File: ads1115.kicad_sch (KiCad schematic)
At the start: 20 parts, among them J29 Conn_02x04_Odd_Even, J30 Conn_01x02, J31 Conn_01x02, J32 Conn_01x02, J33 Conn_01x02, J34 Conn_01x04, U20 ADS1115IDGS

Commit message: WIP v0.2.0 changes
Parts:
- removed J29: Conn_02x04_Odd_Even, HL_Connector_Pad_2.54mm:Pad_2x04_P2.54_1.7x1.7_Rect-Oct, symbol Connector_Generic:Conn_02x04_Odd_Even
- removed J34: Conn_01x04, HL_Connector_Pad_2.54mm:Pad_1x04_P2.54_1.7x1.7_Rect-Oct, symbol Connector_Generic:Conn_01x04
- removed R71, R72, R73, R74: 10k, Resistor_SMD:R_0603_1608Metric_Pad0.98x0.95mm_HandSolder, symbol Device:R
- added J100: Conn_01x05, HL_Connector_Pad_2.54mm:Pad_1x05_P2.54_1.7x1.7_Rect-Oct, symbol Connector_Generic:Conn_01x05
- J27: renamed from J30; footprint HL_Connector_Pad_2.00mm:Pad_1x02_P2.00_1.35x1.35_Oct -> HL_Connector_Pad_2.00mm:Pad_1x02_P2.00_1.35x1.35_Rect-Oct
- J28: renamed from J31; footprint HL_Connector_Pad_2.00mm:Pad_1x02_P2.00_1.35x1.35_Oct -> HL_Connector_Pad_2.00mm:Pad_1x02_P2.00_1.35x1.35_Rect-Oct
- J29: renamed from J32; footprint HL_Connector_Pad_2.00mm:Pad_1x02_P2.00_1.35x1.35_Oct -> HL_Connector_Pad_2.00mm:Pad_1x02_P2.00_1.35x1.35_Rect-Oct
- J30: renamed from J33; footprint HL_Connector_Pad_2.00mm:Pad_1x02_P2.00_1.35x1.35_Oct -> HL_Connector_Pad_2.00mm:Pad_1x02_P2.00_1.35x1.35_Rect-Oct
- R75, R76, R77, R78: value 1k -> 10k; LCSC C17513 -> C17414
- RV10, RV7, RV8, RV9: LCSC (none) -> C118963; THT_LCSC C118963 -> (none)
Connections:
- net AINc0: now also RV7.1, J100.2 (Pin_2); no longer J27.1 (Pin_1), RV7.2
- net AINc1: now also RV8.1, J100.3 (Pin_3); no longer J28.1 (Pin_1), RV8.2
- net AINc2: now also RV9.1, J100.4 (Pin_4); no longer J29.1 (Pin_1), RV9.2
- net AINc3: now also RV10.1, J100.5 (Pin_5); no longer J30.1 (Pin_1), RV10.2
- net AINr0: now also RV7.2; no longer RV7.3
- net AINr1: now also RV8.2; no longer RV8.3
- net AINr2: now also RV9.2; no longer RV9.3
- net AINr3: now also RV10.2; no longer RV10.3
- net GND: now also J27.1 (Pin_1), J28.1 (Pin_1), J29.1 (Pin_1), J30.1 (Pin_1), RV10.3, RV7.3, RV8.3, RV9.3, J100.1 (Pin_1)
- net ALERT/RDY renamed ALERT/RDY
- no-connect marks 4 -> 0
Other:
- moved on the sheet: J27, J28, J29, J30, RV10, RV7, RV8, RV9

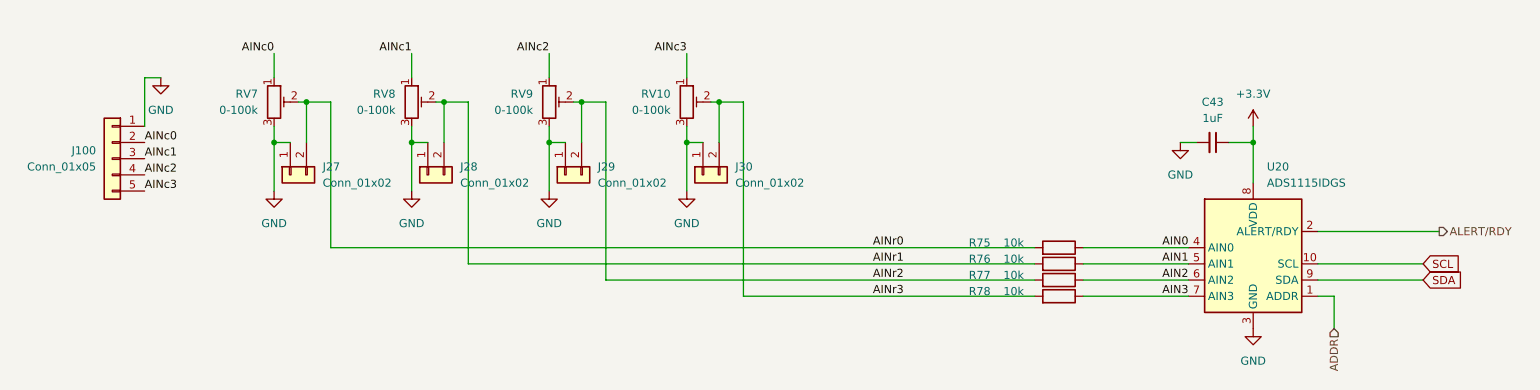
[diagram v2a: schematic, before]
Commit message: Assign part numbers and finish other 0.2.0 changes
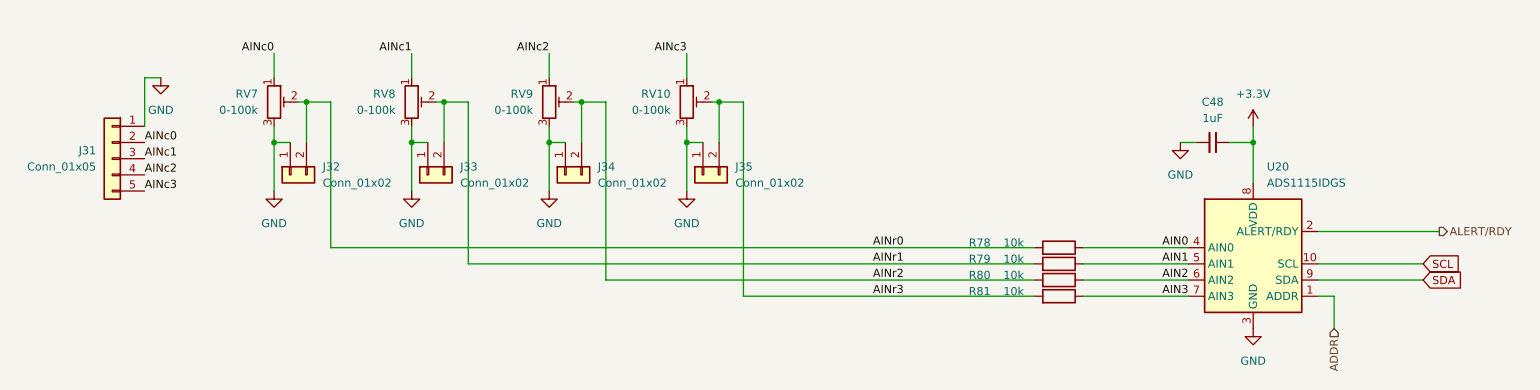
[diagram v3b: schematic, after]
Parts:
- J31: renamed from J100; LCSC (none) -> C492404
- renumbered C43 to C48, J27 to J32, J28 to J33, J29 to J34, J30 to J35, R75 to R78, R76 to R79, R77 to R80, R78 to R81

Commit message: Update the title blocks
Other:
- company: (none) -> Hat Labs Oy
- title: (none) -> HALSPA - Hat Labs Spaghetti Board
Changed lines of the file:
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@@
 	(generator_version "9.0")
 	(paper "A4")
+	(title_block
+		(title "HALSPA - Hat Labs Spaghetti Board")
+		(date "2025-04-17")
+		(rev "v0.2.0")
+		(company "Hat Labs Oy")
+		(comment 1 "See the accompanying LICENSE.md file for license details.")
+	)
 	(junction
 		(at 69.85 74.93)

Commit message: Fix minor production issues
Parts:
- J31: JLCPCB_CORRECTION (none) -> 0;5.08;270
- RV10, RV7, RV8, RV9: now in the parts list
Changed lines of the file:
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@@
 		(unit 1)
 		(exclude_from_sim no)
-		(in_bom no)
+		(in_bom yes)
 		(on_board yes)
 		(dnp no)
@@
 		(unit 1)
 		(exclude_from_sim no)
-		(in_bom no)
+		(in_bom yes)
 		(on_board yes)
 		(dnp no)
@@
 		(unit 1)
 		(exclude_from_sim no)
-		(in_bom no)
+		(in_bom yes)
 		(on_board yes)
 		(dnp no)
@@
 		(unit 1)
 		(exclude_from_sim no)
-		(in_bom no)
+		(in_bom yes)
 		(on_board yes)
 		(dnp no)
@@
 			(at 44.45 77.47 0)
 			(effects
+				(font
+					(size 1.27 1.27)
+				)
+				(hide yes)
+			)
+		)
+		(property "JLCPCB_CORRECTION" "0;5.08;270"
+			(at 44.45 77.47 0)
+			(effects

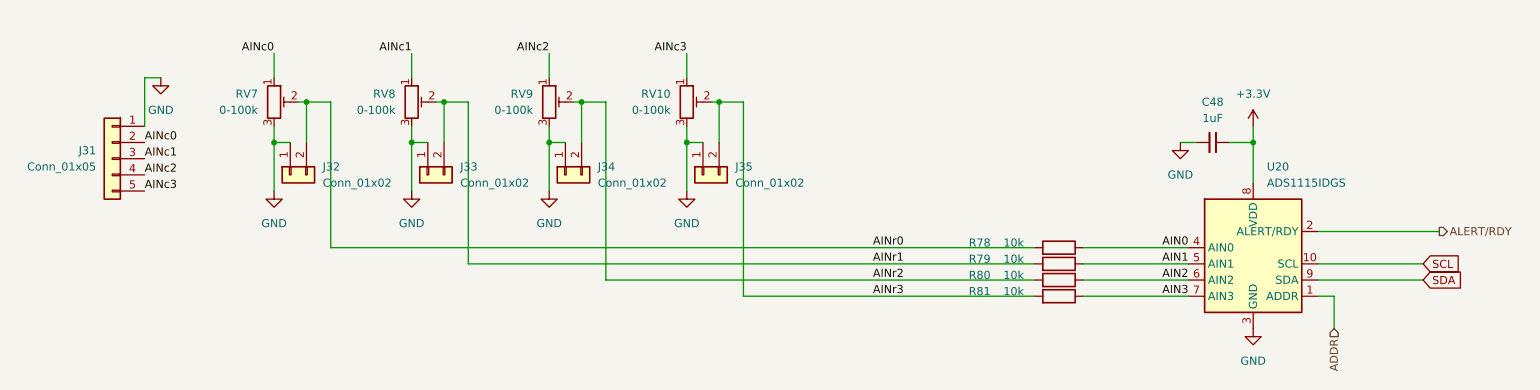
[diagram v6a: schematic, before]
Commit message: Adjust trimmer test pads
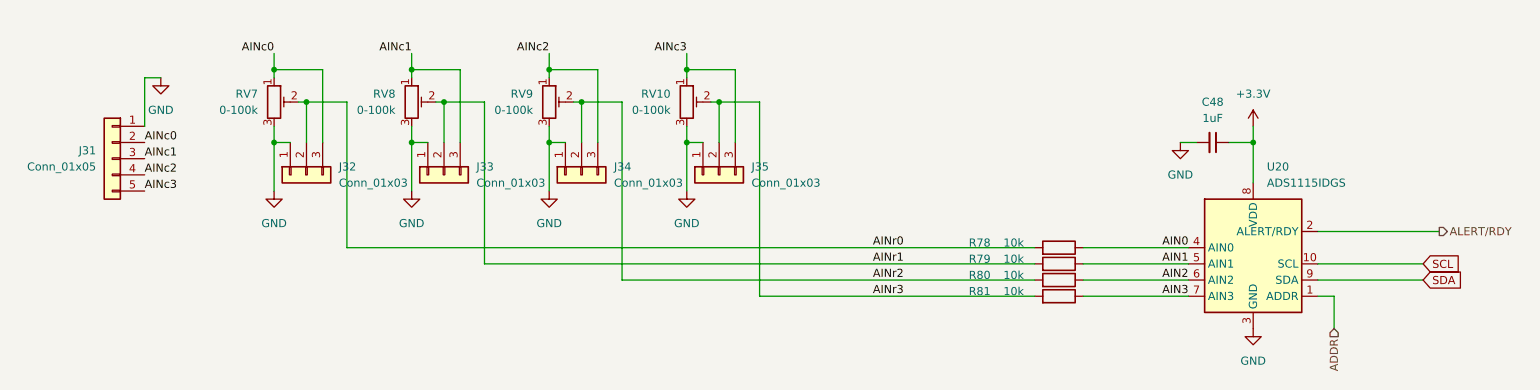
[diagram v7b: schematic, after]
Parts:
- J32, J33, J34, J35: value Conn_01x02 -> Conn_01x03; footprint HL_Connector_Pad_2.00mm:Pad_1x02_P2.00_1.35x1.35_Rect-Oct -> HL_Connector_Pad_2.00mm:Pad_1x03_P2.00_1.35x1.35_Rect-2Oct; symbol Connector_Generic:Conn_01x02 -> Connector_Generic:Conn_01x03
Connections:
- net AINc0: now also J32.3 (Pin_3)
- net AINc1: now also J33.3 (Pin_3)
- net AINc2: now also J34.3 (Pin_3)
- net AINc3: now also J35.3 (Pin_3)

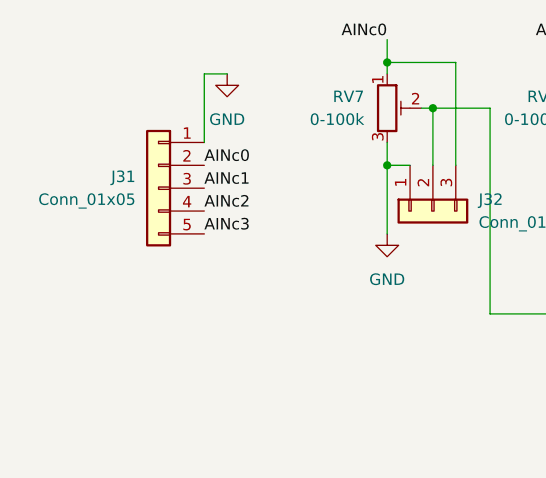
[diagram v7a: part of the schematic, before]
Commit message: Use double row connectors for ADC inputs
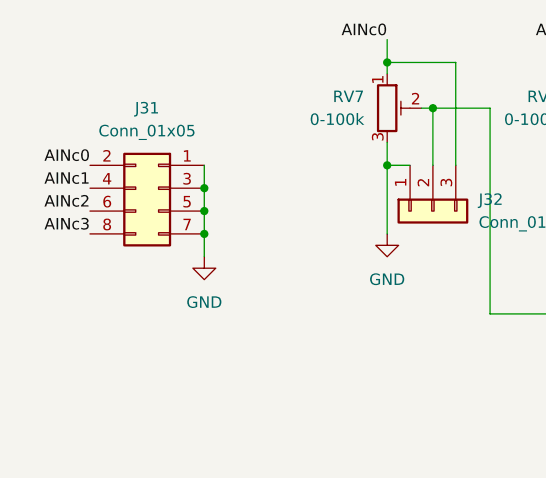
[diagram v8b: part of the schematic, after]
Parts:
- J31: footprint HL_Connector_Pad_2.54mm:Pad_1x05_P2.54_1.7x1.7_Rect-Oct -> HL_Connector_Pad_2.54mm:Pad_2x04_P2.54_1.7x1.7_Rect-Oct; symbol Connector_Generic:Conn_01x05 -> Connector_Generic:Conn_02x04_Odd_Even
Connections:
- net AINc1: now also J31.4 (Pin_4); no longer J31.3 (Pin_3)
- net AINc2: now also J31.6 (Pin_6); no longer J31.4 (Pin_4)
- net AINc3: now also J31.8 (Pin_8); no longer J31.5 (Pin_5)
- net GND: now also J31.3 (Pin_3), J31.5 (Pin_5), J31.7 (Pin_7)
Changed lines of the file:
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@@
+	)
+	(junction
+		(at 49.53 80.01)
+		(diameter 0)
+		(color 0 0 0 0)
 	)
 	(junction
@@
 	)
 	(junction
+		(at 49.53 82.55)
+		(diameter 0)
+		(color 0 0 0 0)
+	)
+	(junction
 		(at 113.03 74.93)
 		(diameter 0)
@@
 	)
 	(junction
+		(at 49.53 77.47)
+		(diameter 0)
+		(color 0 0 0 0)
+	)
+	(junction
 		(at 134.62 74.93)
 		(diameter 0)
@@
 	(wire
 		(pts
+			(xy 49.53 74.93) (xy 49.53 77.47)
+		)
+		(stroke
+			(width 0)
+			(type default)
+		)
+	)
+	(wire
+		(pts
 			(xy 113.03 74.93) (xy 115.57 74.93)
 		)
@@
 	(wire
 		(pts
+			(xy 49.53 82.55) (xy 49.53 85.09)
+		)
+		(stroke
+			(width 0)
+			(type default)
+		)
+	)
+	(wire
+		(pts
 			(xy 69.85 74.93) (xy 69.85 82.55)
 		)
@@
 	(wire
 		(pts
-			(xy 52.07 64.77) (xy 49.53 64.77)
-		)
-		(stroke
-			(width 0)
-			(type default)
-		)
-	)
-	(wire
-		(pts
 			(xy 74.93 68.58) (xy 73.66 68.58)
 		)
@@
 	(wire
 		(pts
-			(xy 49.53 64.77) (xy 49.53 72.39)
-		)
-		(stroke
-			(width 0)
-			(type default)
-		)
-	)
-	(wire
-		(pts
 			(xy 252.73 88.9) (xy 233.68 88.9)
 		)
@@
 	(wire
 		(pts
+			(xy 49.53 77.47) (xy 49.53 80.01)
+		)
+		(stroke
+			(width 0)
+			(type default)
+		)
+	)
+	(wire
+		(pts
 			(xy 116.84 68.58) (xy 118.11 68.58)
 		)
@@
 		(pts
 			(xy 113.03 63.5) (xy 113.03 64.77)
+		)
+		(stroke
+			(width 0)
+			(type default)
+		)
+	)
+	(wire
+		(pts
+			(xy 49.53 80.01) (xy 49.53 82.55)
 		)
 		(stroke
@@
 	)
 	(label "AINc1"
-		(at 49.53 77.47 0)
+		(at 36.83 77.47 180)
 		(effects
 			(font
 				(size 1.27 1.27)
 			)
-			(justify left bottom)
+			(justify right bottom)
 		)
 	)
@@
 	)
 	(label "AINc0"
-		(at 49.53 74.93 0)
+		(at 36.83 74.93 180)
 		(effects
 			(font
 				(size 1.27 1.27)
 			)
-			(justify left bottom)
+			(justify right bottom)
 		)
 	)
@@
 	)
 	(label "AINc2"
-		(at 49.53 80.01 0)
+		(at 36.83 80.01 180)
 		(effects
 			(font
 				(size 1.27 1.27)
 			)
-			(justify left bottom)
+			(justify right bottom)
 		)
 	)
@@
 	)
 	(label "AINc3"
-		(at 49.53 82.55 0)
+		(at 36.83 82.55 180)
 		(effects
 			(font
 				(size 1.27 1.27)
 			)
-			(justify left bottom)
+			(justify right bottom)
 		)
 	)
@@
 	)
 	(symbol
-		(lib_id "Connector_Generic:Conn_01x05")
+		(lib_id "Connector_Generic:Conn_02x04_Odd_Even")
 		(at 44.45 77.47 0)
 		(mirror y)
@@
 		(on_board yes)
 		(dnp no)
+		(fields_autoplaced yes)
 		(property "Reference" "J31"
-			(at 41.91 76.1999 0)
-			(effects
-				(font
-					(size 1.27 1.27)
-				)
-				(justify left)
+			(at 43.18 68.58 0)
+			(effects
+				(font
+					(size 1.27 1.27)
+				)
 			)
 		)
 		(property "Value" "Conn_01x05"
-			(at 41.91 78.7399 0)
-			(effects
-				(font
-					(size 1.27 1.27)
-				)
-				(justify left)
-			)
-		)
-		(property "Footprint" "HL_Connector_Pad_2.54mm:Pad_1x05_P2.54_1.7x1.7_Rect-Oct"
+			(at 43.18 71.12 0)
+			(effects
+				(font
+					(size 1.27 1.27)
+				)
+			)
+		)
+		(property "Footprint" "HL_Connector_Pad_2.54mm:Pad_2x04_P2.54_1.7x1.7_Rect-Oct"
 			(at 44.45 77.47 0)
 			(effects
@@
 			)
 		)
-		(property "Description" "Generic connector, single row, 01x05, script generated (kicad-library-utils/schlib/autogen/connector/)"
+		(property "Description" "Generic connector, double row, 02x04, odd/even pin numbering scheme (row 1 odd numbers, row 2 even numbers), script generated (kicad-library-utils/schlib/autogen/connector/)"
 			(at 44.45 77.47 0)
 			(effects
@@
 		)
 		(pin "1"
+		)
+		(pin "7"
+		)
+		(pin "6"
+		)
+		(pin "8"
 		)
 		(instances
@@
 	(symbol
 		(lib_id "power:GND")
-		(at 52.07 64.77 0)
-		(mirror y)
-		(unit 1)
-		(exclude_from_sim no)
-		(in_bom yes)
-		(on_board yes)
-		(dnp no)
-		(fields_autoplaced yes)
-		(property "Reference" "#PWR0166"
-			(at 52.07 71.12 0)
-			(effects
-				(font
-					(size 1.27 1.27)
-				)
-				(hide yes)
-			)
-		)
-		(property "Value" "GND"
-			(at 52.07 69.85 0)
-			(effects
-				(font
-					(size 1.27 1.27)
-				)
-			)
-		)
-		(property "Footprint" ""
-			(at 52.07 64.77 0)
-			(effects
-				(font
-					(size 1.27 1.27)
-				)
-				(hide yes)
-			)
-		)
-		(property "Datasheet" ""
-			(at 52.07 64.77 0)
-			(effects
-				(font
-					(size 1.27 1.27)
-				)
-				(hide yes)
-			)
-		)
-		(property "Description" "Power symbol creates a global label with name \"GND\" , ground"
-			(at 52.07 64.77 0)
-			(effects
-				(font
-					(size 1.27 1.27)
-				)
-				(hide yes)
-			)
-		)
-		(pin "1"
-		)
-		(instances
-			(project "HALSPA"
-				(path "/7eeba806-440e-4671-bc07-69fe183910a7/f863d577-5163-4667-a0b3-93abcffbcf80/1500ebc1-0d01-4231-ba8c-9a8727fae893"
-					(reference "#PWR0174")
-					(unit 1)
-				)
-				(path "/7eeba806-440e-4671-bc07-69fe183910a7/f863d577-5163-4667-a0b3-93abcffbcf80/e2db82f5-5de5-4c0b-9bb4-4c6c7f22ca6d"
-					(reference "#PWR0166")
-					(unit 1)
-				)
-			)
-		)
-	)
-	(symbol
-		(lib_id "power:GND")
 		(at 212.09 74.93 0)
 		(mirror y)
@@
 					(unit 1)
 				)
+			)
+		)
+	)
+	(symbol
+		(lib_id "power:GND")
+		(at 49.53 85.09 0)
+		(mirror y)
+		(unit 1)
+		(exclude_from_sim no)
+		(in_bom yes)
+		(on_board yes)
+		(dnp no)
+		(fields_autoplaced yes)
+		(property "Reference" "#PWR0166"
+			(at 49.53 91.44 0)
+			(effects
+				(font
+					(size 1.27 1.27)
+				)
+				(hide yes)
+			)
+		)
+		(property "Value" "GND"
+			(at 49.53 90.17 0)
+			(effects
+				(font
+					(size 1.27 1.27)
+				)
+			)
+		)
+		(property "Footprint" ""
+			(at 49.53 85.09 0)
+			(effects
+				(font
+					(size 1.27 1.27)
+				)
+				(hide yes)
+			)
+		)
+		(property "Datasheet" ""
+			(at 49.53 85.09 0)
+			(effects
+				(font
+					(size 1.27 1.27)
+				)
+				(hide yes)
+			)
+		)
+		(property "Description" "Power symbol creates a global label with name \"GND\" , ground"
+			(at 49.53 85.09 0)
+			(effects
+				(font
+					(size 1.27 1.27)
+				)
+				(hide yes)
+			)
+		)
+		(pin "1"
+		)
+		(instances
+			(project "HALSPA"
+				(path "/7eeba806-440e-4671-bc07-69fe183910a7/f863d577-5163-4667-a0b3-93abcffbcf80/1500ebc1-0d01-4231-ba8c-9a8727fae893"
+					(reference "#PWR0174")
+					(unit 1)
+				)
+				(path "/7eeba806-440e-4671-bc07-69fe183910a7/f863d577-5163-4667-a0b3-93abcffbcf80/e2db82f5-5de5-4c0b-9bb4-4c6c7f22ca6d"
+					(reference "#PWR0166")
+					(unit 1)
+				)
